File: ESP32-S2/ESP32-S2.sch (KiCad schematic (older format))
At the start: 39 parts, among them J1 Conn_01x18_Male, J2 Conn_01x21_Male, J3 USB_A, J4 TYPE-C-31-M-12, Q2 L8050QLT1G, Q3 L8050QLT1G, SW1 SW_Push, SW2 SW_Push, U2 ESP32-S2-WROOM-ESP32-S2-WROOM, U3 AMS1117-3.3, U4 CH340C

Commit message: Switches added
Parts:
- SW1, SW2: footprint (none) -> tactile_smd_switch:tactile_smd_switch
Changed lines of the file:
@@
 F 0 "SW1" V 4386 7142 50  0000 R CNN
 F 1 "SW_Push" V 4295 7142 50  0000 R CNN
-F 2 "" H 4340 7390 50  0001 C CNN
+F 2 "tactile_smd_switch:tactile_smd_switch" H 4340 7390 50  0001 C CNN
 F 3 "~" H 4340 7390 50  0001 C CNN
 	1    4340 7190
@@
 F 0 "SW2" V 5486 7147 50  0000 R CNN
 F 1 "SW_Push" V 5395 7147 50  0000 R CNN
-F 2 "" H 5440 7395 50  0001 C CNN
+F 2 "tactile_smd_switch:tactile_smd_switch" H 5440 7395 50  0001 C CNN
 F 3 "~" H 5440 7395 50  0001 C CNN
 	1    5440 7195

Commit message: added 3D models
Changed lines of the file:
@@
 GPIO15
 Wire Wire Line
-	10465 1905 10780 1905
+	10465 2505 10780 2505
+Wire Wire Line
+	10465 2405 10780 2405
+Wire Wire Line
+	10465 2305 10785 2305
+Text Label 10780 2405 2    50   ~ 0
+GPIO35
+Text Label 10785 2305 2    50   ~ 0
+GPIO36
+Wire Wire Line
+	10465 2205 10785 2205
+Wire Wire Line
+	10465 2105 10785 2105
 Wire Wire Line
 	10465 2005 10780 2005
-Wire Wire Line
-	10465 2105 10785 2105
-Text Label 10780 2005 2    50   ~ 0
-GPIO35
-Text Label 10785 2105 2    50   ~ 0
-GPIO36
-Wire Wire Line
-	10465 2205 10785 2205
-Wire Wire Line
-	10465 2305 10785 2305
-Wire Wire Line
-	10465 2405 10780 2405
 Text Label 10785 2205 2    50   ~ 0
 GPIO37
-Text Label 10785 2305 2    50   ~ 0
+Text Label 10785 2105 2    50   ~ 0
 GPIO38
-Text Label 10780 2405 2    50   ~ 0
+Text Label 10780 2005 2    50   ~ 0
 GPIO39
 Wire Wire Line
-	10465 2705 10740 2705
-Wire Wire Line
-	10465 3005 10775 3005
-Wire Wire Line
-	10465 3105 10775 3105
-Text Label 10775 3005 2    50   ~ 0
+	10465 1705 10740 1705
+Wire Wire Line
+	10465 1405 10775 1405
+Wire Wire Line
+	10465 1305 10775 1305
+Text Label 10775 1405 2    50   ~ 0
 GPIO45
-Text Label 10775 3105 2    50   ~ 0
+Text Label 10775 1305 2    50   ~ 0
 GPIO46
 Wire Wire Line
@@
 Wire Wire Line
 	2265 4770 2350 4770
-Text Label 10740 2705 2    50   ~ 0
+Text Label 10740 1705 2    50   ~ 0
 GPIO42
 Text Label 2875 3160 2    50   ~ 0
@@
 L power:VCC #PWR06
 U 1 1 60913688
-P 10465 3205
-F 0 "#PWR06" H 10465 3055 50  0001 C CNN
-F 1 "VCC" V 10480 3333 50  0000 L CNN
-F 2 "" H 10465 3205 50  0001 C CNN
-F 3 "" H 10465 3205 50  0001 C CNN
-	1    10465 3205
-	0    1    1    0
-$EndComp
-Text Label 10780 1905 2    50   ~ 0
+P 10465 1205
+F 0 "#PWR06" H 10465 1055 50  0001 C CNN
+F 1 "VCC" V 10480 1333 50  0000 L CNN
+F 2 "" H 10465 1205 50  0001 C CNN
+F 3 "" H 10465 1205 50  0001 C CNN
+	1    10465 1205
+	0    1    -1   0
+$EndComp
+Text Label 10780 2505 2    50   ~ 0
 GPIO34
-Text Label 10780 1805 2    50   ~ 0
+Text Label 10780 2605 2    50   ~ 0
 GPIO33
-Text Label 10780 1705 2    50   ~ 0
+Text Label 10780 2705 2    50   ~ 0
 GPIO26
 Wire Wire Line
-	10465 1805 10780 1805
-Wire Wire Line
-	10465 1705 10780 1705
-Text Label 10780 1505 2    50   ~ 0
+	10465 2605 10780 2605
+Wire Wire Line
+	10465 2705 10780 2705
+Text Label 10780 2905 2    50   ~ 0
 GPIO21
-Text Label 10785 1405 2    50   ~ 0
+Text Label 10785 3005 2    50   ~ 0
 GPIO20
 Wire Wire Line
-	10465 1505 10780 1505
-Wire Wire Line
-	10465 1405 10785 1405
-Text Label 10820 1305 2    50   ~ 0
+	10465 2905 10780 2905
+Wire Wire Line
+	10465 3005 10785 3005
+Text Label 10820 3105 2    50   ~ 0
 GPIO17
-Text Label 10815 1205 2    50   ~ 0
+Text Label 10815 3205 2    50   ~ 0
 GPIO16
 Wire Wire Line
-	10465 1305 10820 1305
-Wire Wire Line
-	10465 1205 10815 1205
+	10465 3105 10820 3105
+Wire Wire Line
+	10465 3205 10815 3205
 NoConn ~ 2545 1830
 NoConn ~ 2550 1935
@@
 Wire Wire Line
 	9460 1345 9740 1345
-Text Label 10750 2605 2    50   ~ 0
+Text Label 10750 1805 2    50   ~ 0
 SDA
-Text Label 10750 2505 2    50   ~ 0
+Text Label 10750 1905 2    50   ~ 0
 SCL
 Wire Wire Line
-	10465 2605 10750 2605
-Wire Wire Line
-	10465 2505 10750 2505
+	10465 1805 10750 1805
+Wire Wire Line
+	10465 1905 10750 1905
 Wire Wire Line
 	9450 3655 9825 3655
@@
 Text Label 8275 4905 0    50   ~ 0
 VI2
-Text Label 10740 2805 2    50   ~ 0
+Text Label 10740 1605 2    50   ~ 0
 TXD0
-Text Label 10740 2905 2    50   ~ 0
+Text Label 10740 1505 2    50   ~ 0
 RXD0
 Wire Wire Line
-	10465 2805 10740 2805
-Wire Wire Line
-	10465 2905 10740 2905
+	10465 1605 10740 1605
+Wire Wire Line
+	10465 1505 10740 1505
 Wire Wire Line
 	3735 4710 3930 4710
@@
 $EndComp
 Wire Wire Line
-	10465 1605 10770 1605
-Text Label 10770 1605 2    50   ~ 0
+	10465 2805 10770 2805
+Text Label 10770 2805 2    50   ~ 0
 GND
 $Comp

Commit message: Changes in Routing and Silkscreen
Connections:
- net labels added: VBUSC
- wire segments 218 -> 221
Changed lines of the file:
@@
 VI2
 Text Label 8495 5355 0    50   ~ 0
-VBUS
+VBUSC
 Connection ~ 8495 6155
 Wire Wire Line
@@
 Text Label 9825 3655 2    50   ~ 0
 VBUS
-Text Label 3735 5645 0    50   ~ 0
-VBUS
 Wire Wire Line
 	3875 5645 3735 5645
 Wire Wire Line
-	4275 5645 4435 5645
+	4275 5645 4365 5645
 $Comp
 L Device:Polyfuse_Small F1
@@
 	0    -1   -1   0
 $EndComp
+Text Label 3735 5645 0    50   ~ 0
+VBUSC
+Wire Wire Line
+	4365 5645 4365 5825
+Wire Wire Line
+	4365 5825 4825 5825
+Connection ~ 4365 5645
+Wire Wire Line
+	4365 5645 4435 5645
+Text Label 4825 5825 0    50   ~ 0
+VBUS
 $EndSCHEMATC

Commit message: made changes- routing and schematic, added silk screen- pin headers
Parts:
- removed C12: 0.1uF, Capacitor_SMD:C_0603_1608Metric, symbol Device:C
- removed D5: BAT760-7, BAT-760:SOD2513X120N, symbol ESP32-S2-rescue:BAT760-7-BAT760-7
- removed J2: Conn_01x21_Male, Connector_PinHeader_2.54mm:PinHeader_1x21_P2.54mm_Vertical, symbol Connector:Conn_01x21_Male
- added C6: 0.1uF, Capacitor_SMD:C_0603_1608Metric, symbol Device:C
- added J2: Conn_01x22_Male, Connector_PinHeader_2.54mm:PinHeader_1x22_P2.54mm_Vertical, symbol Connector:Conn_01x22_Male
- C13: value 10nF -> 0.1uF
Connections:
- net labels added: VBUSA
- net labels removed: 3V3, VBUS, VCC, VI2, Vin
- wire segments 221 -> 225
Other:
- note added: "AMS1117 5V-3.3V Regulator"
- note added: "SW Pull Up Pins"
- note added: "USB Protection"
- note added: "USB-A\n"
- note added: "USB-C\n"
- note removed: "SSD1306 OLED\n"
- note removed: "USB-A : 5V -> 3.3V using AMS1117\n"
- moved on the sheet: C10, C11, C13, C14, C2, C3, C4, C9, D1, D2, D3, D4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

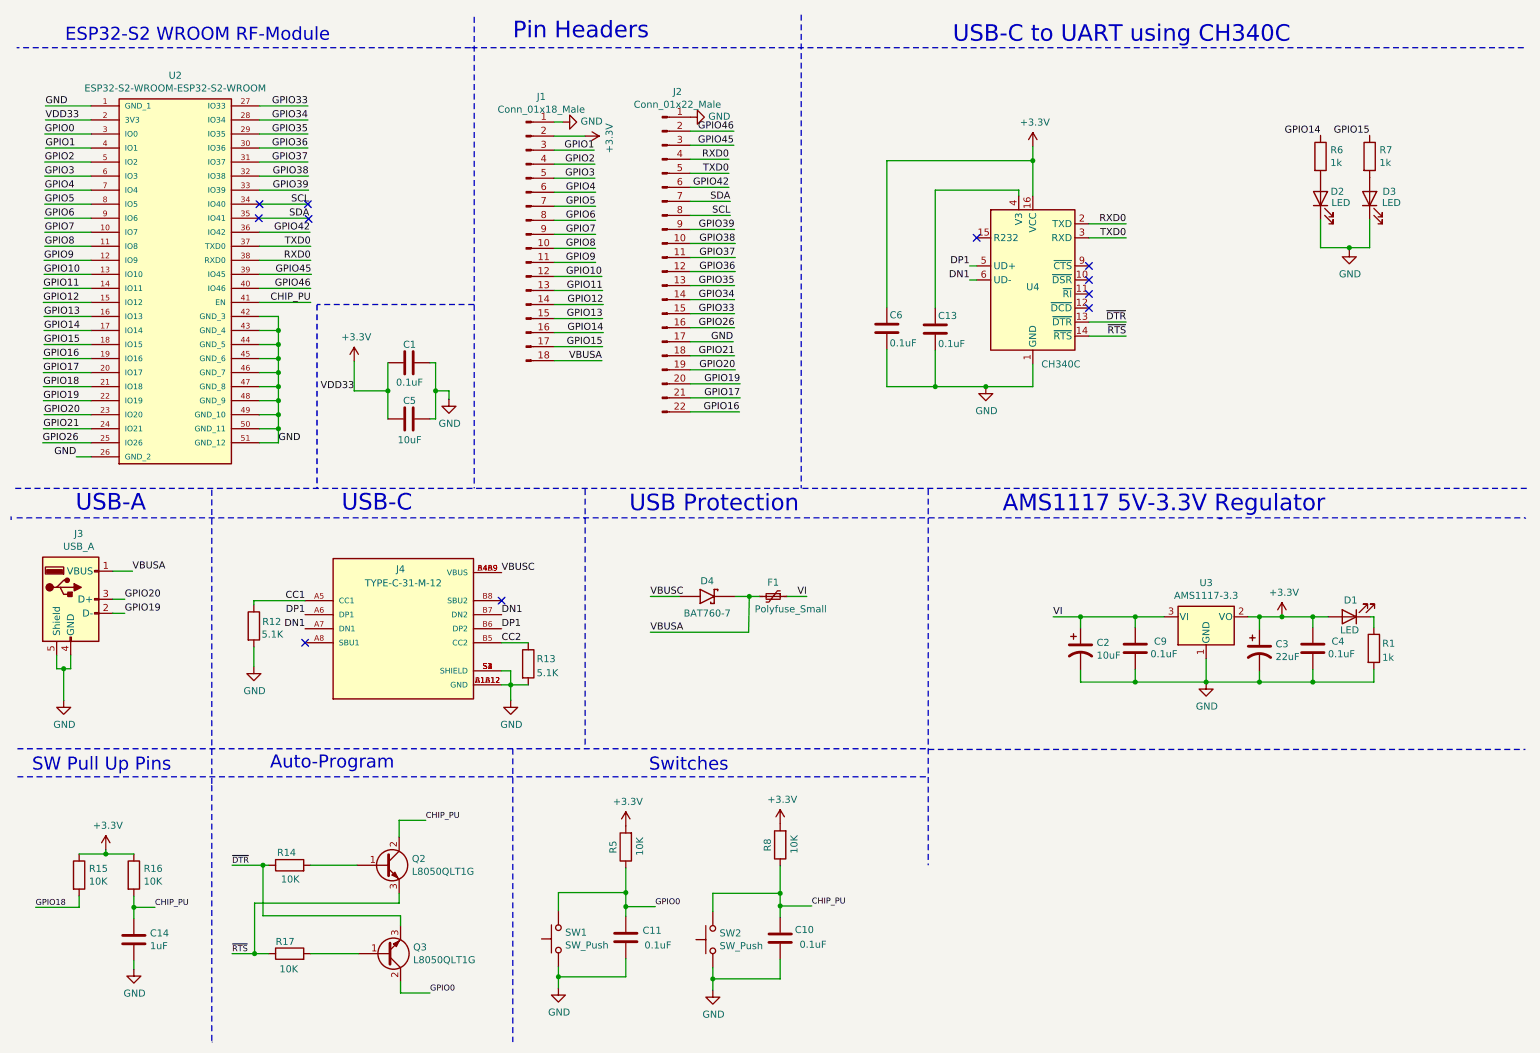
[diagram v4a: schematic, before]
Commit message: added name, corrected annotations
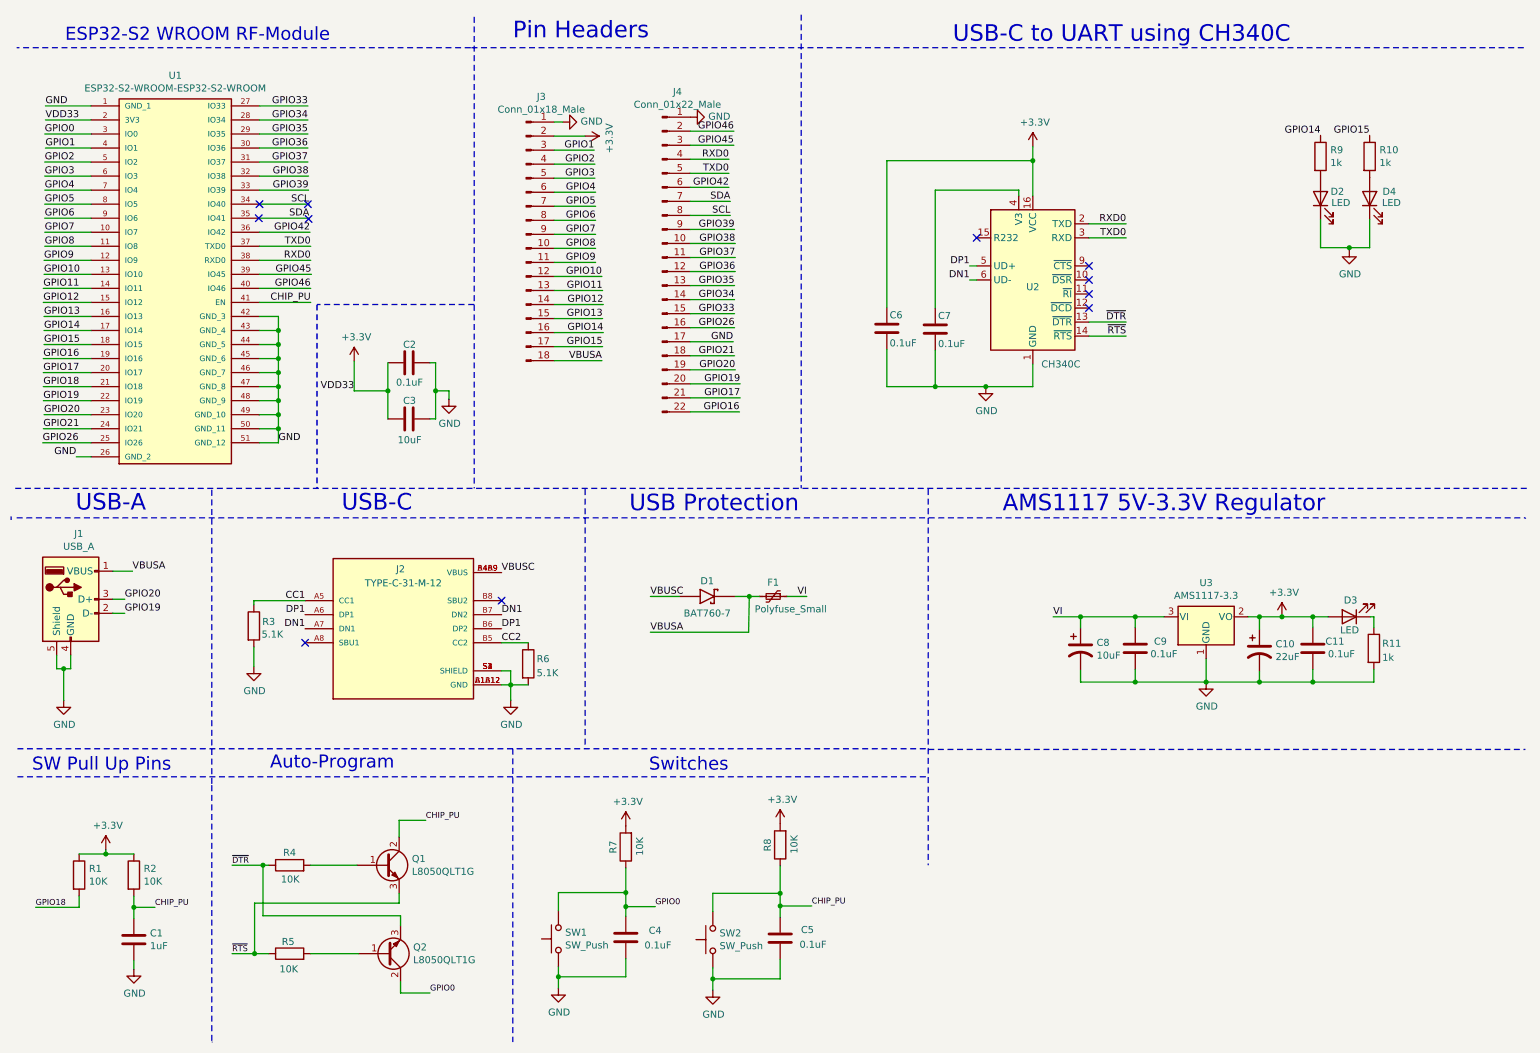
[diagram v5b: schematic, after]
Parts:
- renumbered C14 to C1, C3 to C10, C4 to C11, C1 to C2, C5 to C3, C11 to C4, C10 to C5, C13 to C7, C2 to C8, D4 to D1, D1 to D3, D3 to D4, J3 to J1, J4 to J2, J1 to J3, J2 to J4, Q2 to Q1, Q3 to Q2, R15 to R1, R7 to R10, R1 to R11, R16 to R2, R12 to R3, R14 to R4, R17 to R5, R13 to R6, R5 to R7, R6 to R9, U2 to U1, U4 to U2

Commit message: addedassets, updateed silkscreen
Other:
- moved on the sheet: C2, C3, C6, C7, D2, D4, J3, J4, R10, R9, U2

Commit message: changed Polyfuse package 0603->1206
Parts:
- F1: footprint Fuse:Fuse_0603_1608Metric -> Fuse:Fuse_1206_3216Metric
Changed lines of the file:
@@
 F 0 "F1" V 5760 4625 50  0000 C CNN
 F 1 "Polyfuse_Small" V 5950 4750 50  0000 C CNN
-F 2 "Fuse:Fuse_0603_1608Metric" H 5910 4425 50  0001 L CNN
+F 2 "Fuse:Fuse_1206_3216Metric" H 5910 4425 50  0001 L CNN
 F 3 "~" H 5860 4625 50  0001 C CNN
 	1    5860 4625

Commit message: Finalised kicad design
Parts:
- removed C10: 22uF, Capacitor_SMD:C_0603_1608Metric, symbol Device:CP1
- removed C8: 10uF, Capacitor_SMD:C_0603_1608Metric, symbol Device:CP1
- added C10: 22 uF, Capacitor_SMD:C_0603_1608Metric, symbol Device:C
- added C8: 10 uF, Capacitor_SMD:C_0603_1608Metric, symbol Device:C
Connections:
- net +3V3: now also C10.2
- net GND: now also C10.1, C8.1
- net VI: now also C8.2
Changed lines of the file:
@@
 	0    1    1    0
-$EndComp
-$Comp
-L Device:CP1 C8
-U 1 1 604B949A
-P 8050 5000
-F 0 "C8" H 8165 5046 50  0000 L CNN
-F 1 "10uF" H 8165 4955 50  0000 L CNN
-F 2 "Capacitor_SMD:C_0603_1608Metric" H 8050 5000 50  0001 C CNN
-F 3 "~" H 8050 5000 50  0001 C CNN
-	1    8050 5000
-	1    0    0    -1
 $EndComp
 Wire Wire Line
@@
 Text Label 6100 4625 2    50   ~ 0
 VI
-$Comp
-L Device:CP1 C10
-U 1 1 605D06F3
-P 9325 5010
-F 0 "C10" H 9440 5056 50  0000 L CNN
-F 1 "22uF" H 9440 4965 50  0000 L CNN
-F 2 "Capacitor_SMD:C_0603_1608Metric" H 9325 5010 50  0001 C CNN
-F 3 "~" H 9325 5010 50  0001 C CNN
-	1    9325 5010
-	1    0    0    -1
-$EndComp
 Wire Wire Line
 	9325 4860 9325 4770
@@
 Wire Notes Line
 	4525 2380 4525 2385
+$Comp
+L Device:C C8
+U 1 1 605779A1
+P 8050 5000
+F 0 "C8" H 7825 4950 50  0000 L CNN
+F 1 "10 uF" H 7750 5040 50  0000 L CNN
+F 2 "Capacitor_SMD:C_0603_1608Metric" H 8088 4850 50  0001 C CNN
+F 3 "~" H 8050 5000 50  0001 C CNN
+	1    8050 5000
+	-1   0    0    1
+$EndComp
+$Comp
+L Device:C C10
+U 1 1 60577F9E
+P 9325 5010
+F 0 "C10" H 9100 4960 50  0000 L CNN
+F 1 "22 uF" H 9025 5050 50  0000 L CNN
+F 2 "Capacitor_SMD:C_0603_1608Metric" H 9363 4860 50  0001 C CNN
+F 3 "~" H 9325 5010 50  0001 C CNN
+	1    9325 5010
+	-1   0    0    1
+$EndComp
 $EndSCHEMATC
